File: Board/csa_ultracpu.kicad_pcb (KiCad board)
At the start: 4 copper layers, 160 x 100.1 mm, 175 parts, among them IC13 74244DW, IC14 74LVC14, IC16 74LVC8T245SO24, IC18 74LVC06, IC19 74244DW, IC2 74HCT245DW, IC3 74LVC125, IC4 74HCT245DW, IC5 74HCT245DW, IC6 741G04DBV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

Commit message: more work on r2.1a
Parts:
- C120, C121, C123, U$10, U$11, U$5, U$6, U$8: moved to F.Cu
- USB1: value USB-A-H -> (none)
- moved C120 47.5 mm to (110.5, 114.1), turned to -90 degrees
- moved C121 42.4 mm to (130.7, 114.2), turned to 90 degrees
- moved C25 12.1 mm to (188.0, 90.3), turned to -90 degrees
- moved C55 2.16 mm to (185.1, 78.7)
- moved C123 1.84 mm to (165.0, 70.3), turned to 0 degrees
- moved U$10 1.14 mm to (211.2, 126.5)
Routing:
- net VCC: track 981.2 -> 1024.4 mm, vias 30 -> 31
- net GND: track 915.8 -> 950.8 mm, vias 89 -> 91
- net Net-(U$2B-PROGRAM_B_2): track 53.8 -> 61.9 mm
- net SPI_CLK/CCLK: track 182.2 -> 180.4 mm
- net Net-(D10-PadC): track 29.8 -> 28.6 mm
- net V33: track 1119.9 -> 1120.9 mm, vias 63 -> 64
- net RAMD5: track 25.4 -> 26.3 mm
- net D2: track 89.5 -> 90.4 mm
- net VSYNC: track 143.0 -> 142.2 mm
- net /A/V Out/VERTICAL: track 41.9 -> 41.2 mm
- net A14: track 122.8 -> 122.1 mm
- net A8: track 88.8 -> 88.1 mm
- net /CPU,RAM,ROM/PET_VSYNC: track 102.4 -> 103.0 mm
- net RAMD4: track 24.1 -> 24.7 mm
- net SPI_MISO/DIN: track 183.7 -> 184.3 mm
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
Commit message: more work on r2.1a - only bom xls is missing/outdated
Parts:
- C121: value 1u -> 0.1u
- C9: value 1.0u Cer -> 1u
- D9: value 1N4148 -> 1N4448
- USB1: value (none) -> USB-A-H
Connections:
- U$2 pad 67: SPI_IN3 -> RAMD0
- U$2 pad 69: RAMD0 -> RAMD7
- U$2 pad 75: RAMD7 -> SPI_IN3
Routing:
- net V33: track 1120.9 -> 1171.5 mm, vias 64 -> 65
- net GND: track 950.8 -> 941.5 mm
- net SPI_IN3: track 32.1 -> 37.3 mm
- net VCC: track 1024.4 -> 1019.5 mm
- net RAMD7: track 29.0 -> 24.5 mm
- net A14: track 122.1 -> 119.8 mm
- net /BUS I/O/BR/-W: track 30.5 -> 28.3 mm
- net /LDAC: track 118.8 -> 116.6 mm
- net BE_IN: track 83.1 -> 80.9 mm
- net /BUS I/O//BNMI: track 97.6 -> 95.5 mm
- net /IRQ: track 255.5 -> 253.6 mm
- net R/-W: track 148.2 -> 146.3 mm
- net A12: track 115.1 -> 113.2 mm
- net /A/V Out/IBLUE: track 29.5 -> 27.6 mm
- net SPI_MOSI: track 152.0 -> 150.1 mm
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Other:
- board text added: "(C) 2024 A. Fachat"
- board text removed: "(C) 2023 A. Fachat"

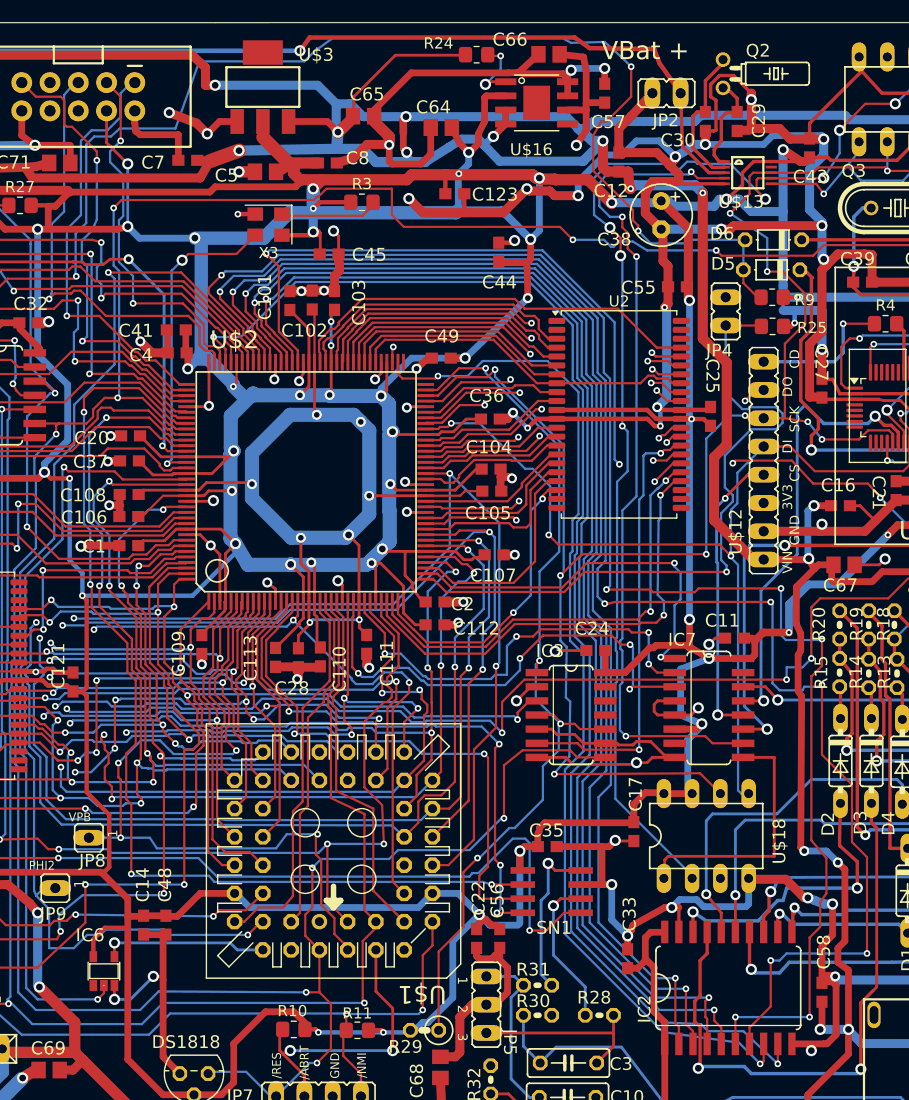
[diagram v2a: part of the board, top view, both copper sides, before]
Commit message: add Flash ROM type prints on PCB
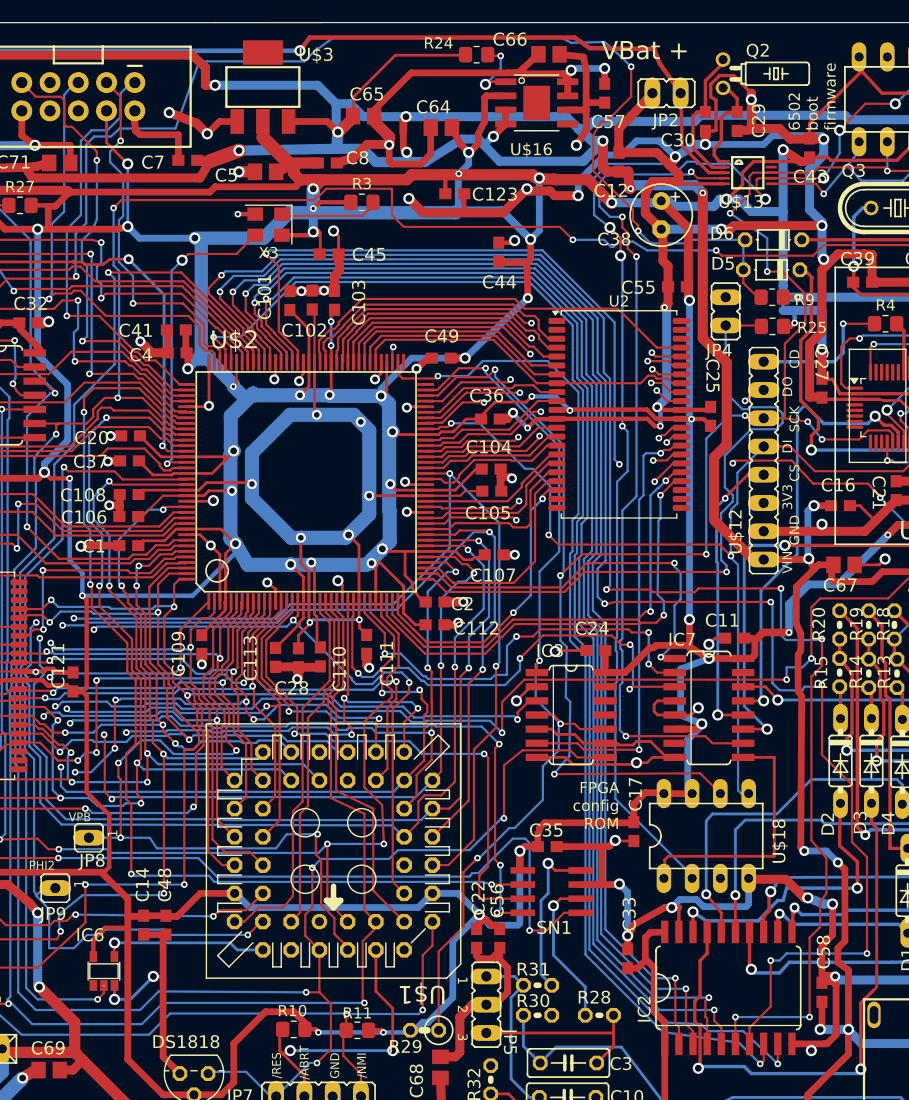
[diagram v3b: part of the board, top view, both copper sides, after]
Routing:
- net V33: track 1171.5 -> 1181.1 mm, vias 65 -> 67
- net IGOUT: track 93.5 -> 92.1 mm
- net IBOUT: track 112.1 -> 110.8 mm
- net IROUT: track 120.2 -> 118.9 mm
- net BOUT: track 113.8 -> 112.5 mm
- net GOUT: track 113.4 -> 112.2 mm
- net A12: track 113.2 -> 112.1 mm
- net ROUT: track 114.1 -> 113.2 mm
- net A15: track 94.4 -> 93.9 mm
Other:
- board text added: "6502 boot firmware"
- board text added: "FPGA config ROM"
